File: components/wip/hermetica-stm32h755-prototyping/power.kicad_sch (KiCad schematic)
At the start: 29 parts, among them J2 DRONE-SERVO-HEADER, J28 GCT-USB3075-30-A, J3 Conn_01x01, U5 LM66100DCK, U7 LD1117S50TR_SOT223, U8 LM66100DCK

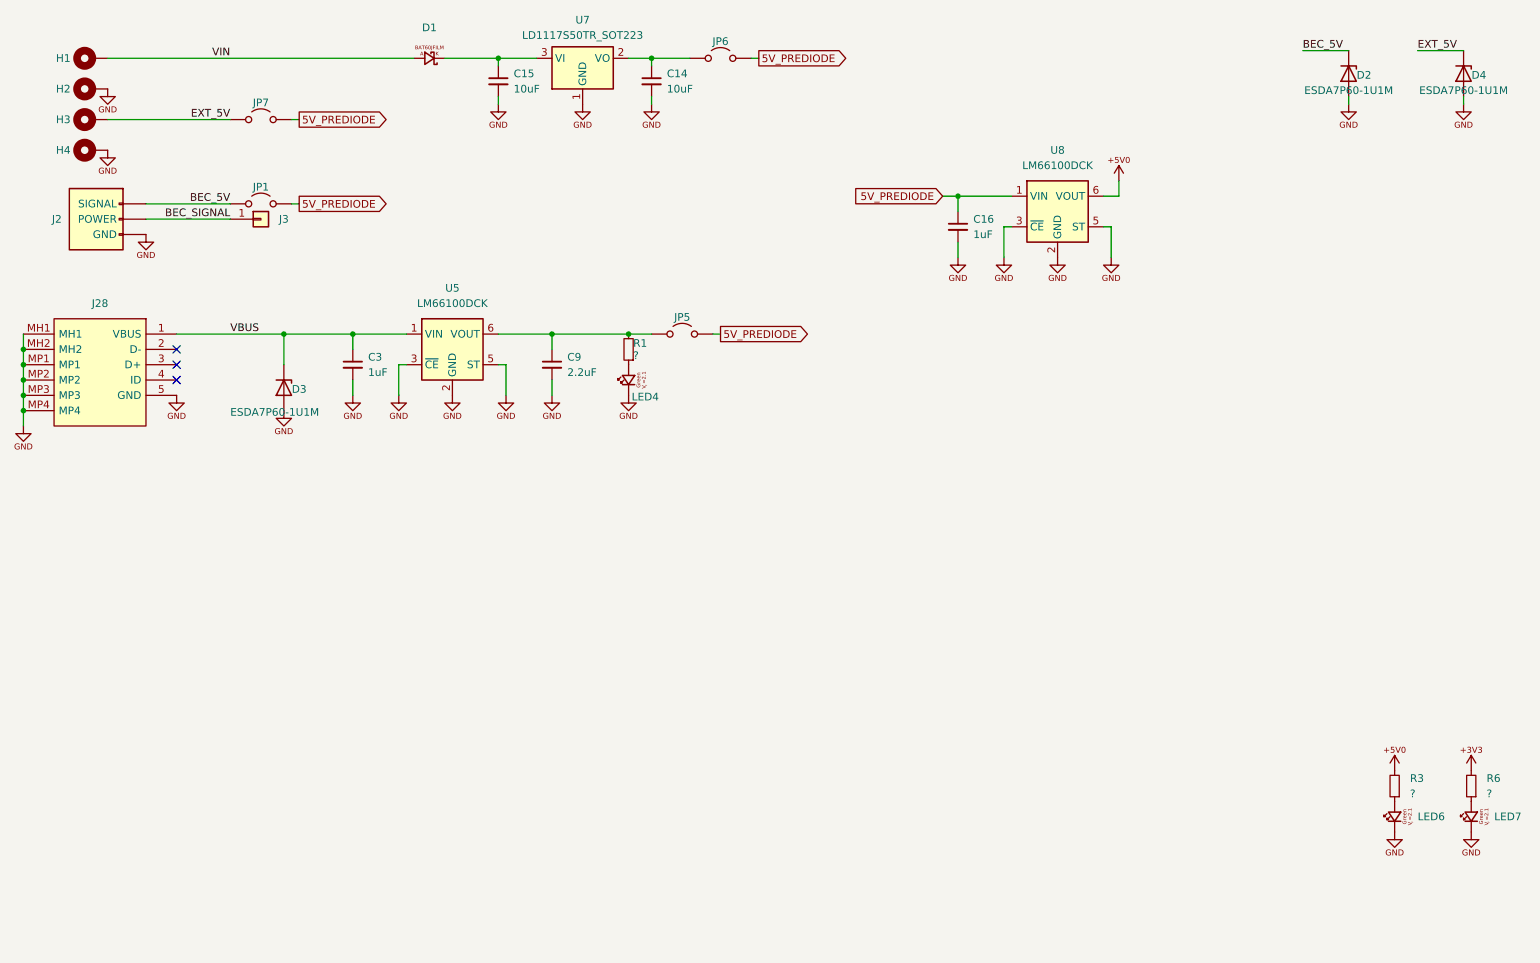
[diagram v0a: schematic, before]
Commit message: STM32H755ZIT6 dev board
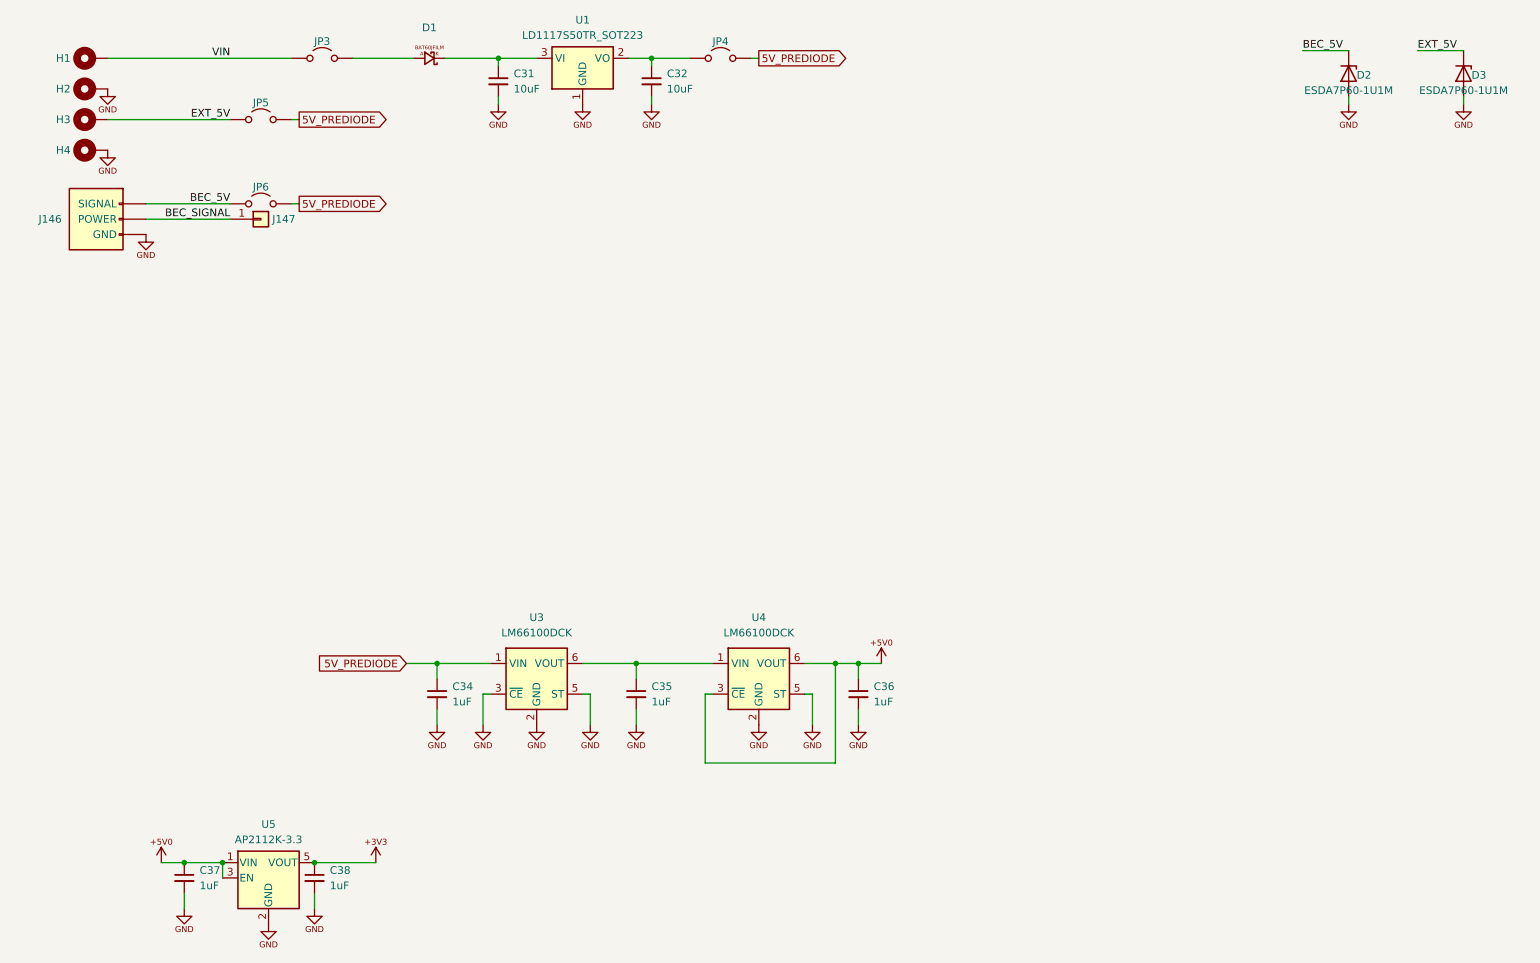
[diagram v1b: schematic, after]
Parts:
- removed C16, C3: 1uF, djStandard:C_0402_1005Metric, symbol DJ:C
- removed C9: 2.2uF, djStandard:C_0402_1005Metric, symbol DJ:C
- removed D3: ESDA7P60-1U1M, djStandard:STM-ESDA7P60-1U1M, symbol DJ:STM-ESDA7P60-1U1M
- removed J28: GCT-USB3075-30-A, djStandard:GCT-USB3075-30-A, symbol DJ:GCT-USB3075-30-A
- removed JP5: Jumper_2_Open, djStandard:CONNECTOR-PCB-HANDSOLDER-01X02-MALE, symbol Jumper:Jumper_2_Open
- removed LED4: KINGBRIGHT-LED-0402-GREEN, djStandard:KINGBRIGHT-LED-APHHS1005-0402, symbol DJ:KINGBRIGHT-LED-0402-GREEN
- removed LED6, LED7: KINGBRIGHT-LED-0402-ORANGE, djStandard:KINGBRIGHT-LED-APHHS1005-0402, symbol DJ:KINGBRIGHT-LED-0402-GREEN
- removed R1, R3, R6: ?, djStandard:R_0402_1005Metric, symbol DJ:R
- removed U5, U8: LM66100DCK, Package_TO_SOT_SMD:SOT-363_SC-70-6, symbol Power_Management:LM66100DCK
- added C34, C35, C36: 1uF, djStandard:C_0603_1608Metric, symbol DJ:C
- added C37, C38: 1uF, djStandard:C_0805_2012Metric, symbol DJ:C
- added JP3: Jumper_2_Open, djStandard:CONNECTOR-PCB-HANDSOLDER-01X02-MALE, symbol Jumper:Jumper_2_Open
- added U3, U4: LM66100DCK, Package_TO_SOT_SMD:SOT-363_SC-70-6, symbol Power_Management:LM66100DCK
- added U5: AP2112K-3.3, Package_TO_SOT_SMD:SOT-23-5, symbol Regulator_Linear:AP2112K-3.3
- renumbered C15 to C31, C14 to C32, D4 to D3, J2 to J146, J3 to J147, JP6 to JP4, JP7 to JP5, JP1 to JP6, U7 to U1
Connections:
- net +3V3: now also C38.1, U5.5 (VOUT)
- net +5V0: now also C36.1, C37.1, U4.3 (~{CE}), U4.6 (VOUT), U5.1 (VIN), U5.3 (EN)
- net 5V_PREDIODE: now also C34.1, U3.1 (VIN)
- net GND: now also C34.2, C35.2, C36.2, C37.2, C38.2, U3.2 (GND), U3.3 (~{CE}), U3.5 (ST), U4.2 (GND), U4.5 (ST), U5.2 (GND)
- net VIN: now also JP3.1 (A); no longer D1.2 (A)
- new net: C35.1, U3.6 (VOUT), U4.1 (VIN)
- new net: D1.2 (A), JP3.2 (B)
- no-connect marks 3 -> 0
